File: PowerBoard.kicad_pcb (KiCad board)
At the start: 2 copper layers, 212 parts, among them Q1 PSMN020-100YS, Q2 PSMN020-100YS, Q3 PSMN020-100YS, Q4 PSMN020-100YS, Q5 PSMN020-100YS, U1 LT8342RV-TRMPBF, U10 LM5050-1, U11 PINA745AIRELR, U12 TPS16851VMAR, U13 LM5050-1, U14 TPS16851VMAR, U15 LM5050-1, U16 TPS16851VMAR, U17 LM5050-1, U18 LMR43620MSC5RPERQ1, U2 AD5259BRMZ100, U3 ADAFRUIT_QT_PY, U4 TPS16851VMAR, U5 LM5050-1, U6 LT8342RV-TRMPBF, U7 PINA745AIRELR, U8 AD5259BRMZ100, U9 TPS16851VMAR

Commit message: Starting bus load switch layout
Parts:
- removed D13, D17, D18, D5: TPSMB28CA-VR, Diode_SMD:D_SMB
- removed D15, D19, D20, D3, D7: BAT46GWJ, Diode_SMD:D_SOD-123
- removed L1: 33uH, _Power_Board:IND_SER2918H-333KL
- removed L3: 3.3uH, Inductor_SMD:L_Bourns_SRN6045TA
- removed Q3, Q4, Q5: PSMN020-100YS, Package_TO_SOT_SMD:LFPAK56
- removed R25: 274k, Resistor_SMD:R_0603_1608Metric
- removed R26, R39: 1Meg, Resistor_SMD:R_0603_1608Metric
- removed R38, R64: 100, Resistor_SMD:R_0603_1608Metric
- removed R40, R66: 36k, Resistor_SMD:R_0603_1608Metric
- removed R42, R68: 67.3k, Resistor_SMD:R_0603_1608Metric
- removed R44: 240k, Resistor_SMD:R_0603_1608Metric
- removed R45: 33k, Resistor_SMD:R_0603_1608Metric
- removed R49, R62: 1k, Resistor_SMD:R_0603_1608Metric
- removed R50, R63: 10, Resistor_SMD:R_1206_3216Metric
- removed R69: 150, Resistor_SMD:R_0603_1608Metric
- removed U1, U6: LT8342RV-TRMPBF, _Power_Board:05-08-7040_ADI
- removed U12, U4: TPS16851VMAR, _Power_Board:05-08-7040_ADI
- removed U17, U5: LM5050-1, Package_TO_SOT_SMD:TSOT-23-6
- removed U18: LMR43620MSC5RPERQ1, _Power_Board:RPE0009A-MFG
- removed U2: AD5259BRMZ100, _Power_Board:RM_10_ADI
- removed U3: ADAFRUIT_QT_PY, _Power_Board:MODULE_ADAFRUIT_QT_PY
- removed U7: PINA745AIRELR, _Power_Board:REL0014A_PINA745AIRELR_TEX
- added C86: 1uF, Capacitor_SMD:C_0603_1608Metric, F.Cu at (43.5, 77.2)
- added C87: 0.1uF, Capacitor_SMD:C_0603_1608Metric, F.Cu at (43.5, 79.7)
- added C88: 1uF, Capacitor_SMD:C_0603_1608Metric, F.Cu at (82.0, 76.0)
- added C89: 0.1uF, Capacitor_SMD:C_0603_1608Metric, F.Cu at (82.0, 78.5)
- added FB5: FerriteBead, Inductor_SMD:L_1812_4532Metric, F.Cu at (81.1, 52.4)
- added J1: Conn_01x02_Socket, Connector_JST:JST_PH_B2B-PH-K_1x02_P2.00mm_Vertical, F.Cu at (67.0, 87.3)
- added NT1: NetTie_2, NetTie:NetTie-2_SMD_Pad0.5mm, F.Cu at (173.8, 85.7)
- added NT2: NetTie_2, NetTie:NetTie-2_SMD_Pad0.5mm, F.Cu at (173.8, 87.2)
- added NT3: NetTie_2, NetTie:NetTie-2_SMD_Pad0.5mm, F.Cu at (88.7, -14.2)
- added NT4: NetTie_2, NetTie:NetTie-2_SMD_Pad0.5mm, F.Cu at (173.8, 98.5)
- added NT5: NetTie_2, NetTie:NetTie-2_SMD_Pad0.5mm, F.Cu at (173.8, 100.0)
- added NT6: NetTie_2, NetTie:NetTie-2_SMD_Pad0.5mm, F.Cu at (62.9, 47.2)
- added Q19: PSMN020-100YS, Package_TO_SOT_SMD:LFPAK56, F.Cu at (190.7, 104.0)
- added Q9: PSMN020-100YS, Package_TO_SOT_SMD:LFPAK56, F.Cu at (190.7, 91.2)
- added TP2: TP_PGOOD, TestPoint:TestPoint_Plated_Hole_D5.0mm, F.Cu at (210.1, 22.5)
- added TP3: TP_FLTn, TestPoint:TestPoint_Plated_Hole_D5.0mm, F.Cu at (220.7, 22.8)
- C19: value 100nF -> 100 nF; footprint Capacitor_SMD:C_1206_3216Metric -> Capacitor_SMD:C_0402_1005Metric
- C2: value 3.3nF -> 100nF
- C20: value 100pF -> 100 nF; footprint Capacitor_SMD:C_0603_1608Metric -> Capacitor_SMD:C_0402_1005Metric
- C21: value 10pF -> 100 nF; footprint Capacitor_SMD:C_0603_1608Metric -> Capacitor_SMD:C_0402_1005Metric
- C22: value 0.22uF -> 100 nF; footprint Capacitor_SMD:C_0603_1608Metric -> Capacitor_SMD:C_0402_1005Metric
- C23: value 4.7nF -> 100 nF; footprint Resistor_SMD:R_0603_1608Metric -> Capacitor_SMD:C_0402_1005Metric
- C24: value 22pF -> 100 nF; footprint Capacitor_SMD:C_0603_1608Metric -> Capacitor_SMD:C_0402_1005Metric
- C25: value 100pF -> 15p; footprint Capacitor_SMD:C_0603_1608Metric -> Resistor_SMD:R_0201_0603Metric
- C26: value 22nF -> 15p; footprint Capacitor_SMD:C_0805_2012Metric -> Resistor_SMD:R_0201_0603Metric
- C27: value 100nF -> 100 nF; footprint Capacitor_SMD:C_0805_2012Metric -> Capacitor_SMD:C_0402_1005Metric
- C28: value 220pF -> 100 nF; footprint Capacitor_SMD:C_0603_1608Metric -> Capacitor_SMD:C_0402_1005Metric
- C29: value 3.3nF -> 100 nF; footprint Capacitor_SMD:C_0603_1608Metric -> Capacitor_SMD:C_0402_1005Metric
- C3, C37: value 100nF -> 10uF; footprint Capacitor_SMD:C_0603_1608Metric -> Capacitor_SMD:C_0805_2012Metric
- C30, C32, C34: value 100nF -> 4.7u; footprint Capacitor_SMD:C_0603_1608Metric -> Capacitor_SMD:C_0402_1005Metric
- C31: value 2.2uF -> 100 nF; footprint Capacitor_SMD:C_0603_1608Metric -> Capacitor_SMD:C_0402_1005Metric
- C33: value 10uF -> 4.7u; footprint Capacitor_SMD:C_0805_2012Metric -> Capacitor_SMD:C_0402_1005Metric
- C35: value 33uF -> 220pF; footprint Capacitor_SMD:CP_Elec_6.3x5.8 -> Capacitor_SMD:C_0603_1608Metric
- C36, C41, C46: value 10uF -> 100nF; footprint Capacitor_SMD:C_0805_2012Metric -> Capacitor_SMD:C_0603_1608Metric
- C38: value 100nF -> 3.3nF
- C4: value 2.2uF -> 3.3nF
- C40, C6: value 10uF -> 2.2uF; footprint Capacitor_SMD:C_0805_2012Metric -> Capacitor_SMD:C_0603_1608Metric
- C42: value 100nF -> 33uF; footprint Capacitor_SMD:C_0603_1608Metric -> Capacitor_SMD:CP_Elec_6.3x5.8
- C43: value 220pF -> 10uF; footprint Capacitor_SMD:C_0603_1608Metric -> Capacitor_SMD:C_0805_2012Metric
- C47: value 100pF -> 10uF; footprint Capacitor_SMD:C_0603_1608Metric -> Capacitor_SMD:C_0805_2012Metric
- C48: value 10pF -> 10uF; footprint Capacitor_SMD:C_0603_1608Metric -> Capacitor_SMD:C_0805_2012Metric
- C49: value 0.22uF -> 100nF
- C50: value 4.7nF -> 220pF; footprint Resistor_SMD:R_0603_1608Metric -> Capacitor_SMD:C_0603_1608Metric
- C51: value 22pF -> 100nF
- C52: value 100pF -> 100nF
- C53: value 22nF -> 10uF
- C54: footprint Capacitor_SMD:C_0805_2012Metric -> Capacitor_SMD:C_0603_1608Metric
- C55: footprint Capacitor_SMD:C_0603_1608Metric -> Capacitor_SMD:C_0805_2012Metric
- C56: value 100pF -> 100nF; footprint Capacitor_SMD:C_0603_1608Metric -> Capacitor_SMD:C_0805_2012Metric
- C57: value 10pF -> 100nF; footprint Capacitor_SMD:C_0603_1608Metric -> Capacitor_SMD:C_0805_2012Metric
- C58: value 0.22uF -> 100pF; moved to B.Cu
- C59: value 4.7nF -> 10pF; footprint Resistor_SMD:R_0603_1608Metric -> Capacitor_SMD:C_0603_1608Metric; moved to B.Cu
- C60: value 22pF -> 0.22uF
- C61: value 100pF -> 4.7nF; footprint Capacitor_SMD:C_0603_1608Metric -> Resistor_SMD:R_0603_1608Metric; moved to B.Cu
- C62: value 22nF -> 22pF; footprint Capacitor_SMD:C_0805_2012Metric -> Capacitor_SMD:C_0603_1608Metric; moved to B.Cu
- C63: value 100nF -> 100pF; footprint Capacitor_SMD:C_0805_2012Metric -> Capacitor_SMD:C_0603_1608Metric; moved to B.Cu
- C64: value 100pF -> 22nF; footprint Capacitor_SMD:C_0603_1608Metric -> Capacitor_SMD:C_0805_2012Metric; moved to B.Cu
- C65: value 10pF -> 100nF; moved to B.Cu
- C66: value 0.22uF -> 10uf; footprint Capacitor_SMD:C_0603_1608Metric -> Capacitor_SMD:C_1210_3225Metric
- C67, C75: value 4.7nF -> 1uF; footprint Resistor_SMD:R_0603_1608Metric -> Capacitor_SMD:C_0603_1608Metric
- C68: value 22pF -> 10uf; footprint Capacitor_SMD:C_0603_1608Metric -> Capacitor_SMD:C_1210_3225Metric
- C69: value 100pF -> 10uf; footprint Capacitor_SMD:C_0603_1608Metric -> Capacitor_SMD:C_1210_3225Metric
- C70: value 22nF -> 1uF; footprint Capacitor_SMD:C_0805_2012Metric -> Capacitor_SMD:C_0603_1608Metric
- C71: value 100nF -> 1uF; footprint Capacitor_SMD:C_0805_2012Metric -> Capacitor_SMD:C_0603_1608Metric
- C72: value 100pF -> 1uF
- C73: value 10pF -> 10nF
- C74: value 0.22uF -> 0.1uF
- C76: value 22pF -> 4.7pF
- C77: value 100pF -> 47uF; footprint Capacitor_SMD:C_0603_1608Metric -> Capacitor_SMD:C_1210_3225Metric
- C78: value 22nF -> 100pF; footprint Capacitor_SMD:C_0805_2012Metric -> Capacitor_SMD:C_0603_1608Metric; moved to B.Cu
- C79: value 100nF -> 10pF; footprint Capacitor_SMD:C_0805_2012Metric -> Capacitor_SMD:C_0603_1608Metric; moved to B.Cu
- C80: value 4.7uF -> 0.22uF; footprint Capacitor_SMD:C_0805_2012Metric -> Capacitor_SMD:C_0603_1608Metric
- C81: value 100nF -> 4.7nF; footprint Capacitor_SMD:C_0603_1608Metric -> Resistor_SMD:R_0603_1608Metric; moved to B.Cu
- C82: value 1uF -> 22pF; footprint Capacitor_SMD:C_0805_2012Metric -> Capacitor_SMD:C_0603_1608Metric; moved to B.Cu
- C83: value 100nF -> 100pF; moved to B.Cu
- C84: value 22uF -> 22nF; footprint Capacitor_SMD:CP_Elec_6.3x5.9 -> Capacitor_SMD:C_0805_2012Metric; moved to B.Cu
- C85: value 22uF -> 100nF; footprint Capacitor_SMD:CP_Elec_6.3x5.9 -> Capacitor_SMD:C_0603_1608Metric; moved to B.Cu
- D10: value TPSMB28CA-VR -> SMF5.0A; footprint Diode_SMD:D_SMB -> Diode_SMD:D_SOD-123F
- D11, D12: value BAT46GWJ -> TPSMB28CA-VR; footprint Diode_SMD:D_SOD-123 -> Diode_SMD:D_SMB
- D14, D6: value TPSMB28CA-VR -> BAT46GWJ; footprint Diode_SMD:D_SMB -> Diode_SMD:D_SOD-123
- D8: value BAT46GWJ -> SMCJ26A; footprint Diode_SMD:D_SOD-123 -> Diode_SMD:D_SMC
- D9: value TPSMB28CA-VR -> SMF3.3; footprint Diode_SMD:D_SMB -> Diode_SMD:D_SOD-123F
- L2: value 33uH -> 3.3u; footprint _Power_Board:IND_SER2918H-333KL -> Inductor_SMD:L_0805_2012Metric
- Q1, Q2: value PSMN020-100YS -> Q_NMOS; footprint Package_TO_SOT_SMD:LFPAK56 -> Package_DFN_QFN:WDFN-8-1EP_2x2.2mm_P0.5mm_EP0.80x0.54
- R10: value 1Meg -> 33k; footprint Resistor_SMD:R_0603_1608Metric -> Resistor_SMD:R_0402_1005Metric
- R11: value 67.3k -> 1k; footprint Resistor_SMD:R_0603_1608Metric -> Resistor_SMD:R_0402_1005Metric
- R12: value 150 -> 1k; footprint Resistor_SMD:R_0603_1608Metric -> Resistor_SMD:R_0201_0603Metric
- R13: value 240k -> 1k; footprint Resistor_SMD:R_0603_1608Metric -> Resistor_SMD:R_0402_1005Metric
- R14, R15: value 33k -> 27; footprint Resistor_SMD:R_0603_1608Metric -> Resistor_SMD:R_0201_0603Metric
- R16: value 1.26k -> 33; footprint Resistor_SMD:R_0603_1608Metric -> Resistor_SMD:R_0402_1005Metric
- R17: value 464 -> 33.6k
- R18: value 1k -> 60.4k
- R19: value 10 -> 33.6k; footprint Resistor_SMD:R_1206_3216Metric -> Resistor_SMD:R_0603_1608Metric
- R20: value 100 -> R_US
- R21: value 33.6k -> 274k
- R22: value 60.4k -> 15k
- R23: value 33.6k -> 33k
- R24: value 15k -> 33k
- R27, R53: value 36k -> 1Meg; moved to B.Cu
- R28, R52: value 1Meg -> 36k; moved to B.Cu
- R29: value 67.3k -> 1Meg; moved to B.Cu
- R30: value 150 -> 67.3k; moved to B.Cu
- R31: value 240k -> 150
- R32: value 33k -> 240k; moved to B.Cu
- R33, R58, U10: moved to B.Cu
- R34: value 1.26k -> 33k; moved to B.Cu
- R35: value 464 -> 1.26k; moved to B.Cu
- R36: value 1k -> 464; moved to B.Cu
- R37: value 10 -> 1k; footprint Resistor_SMD:R_1206_3216Metric -> Resistor_SMD:R_0603_1608Metric; moved to B.Cu
- R4: value 15k -> R_US
- R41, R65: value 1Meg -> 10; footprint Resistor_SMD:R_0603_1608Metric -> Resistor_SMD:R_1206_3216Metric
- R43: value 150 -> 100; moved to B.Cu
- R46: value 33k -> 18.22K
- R47: value 1.26k -> 1M
- R48: value 464 -> 243k
- R51: value 100 -> 1Meg; moved to B.Cu
- R54: value 1Meg -> 67.3k; moved to B.Cu
- R55: value 67.3k -> 150
- R56: value 150 -> 240k; moved to B.Cu
- R57: value 240k -> 33k; moved to B.Cu
- R59: value 33k -> 1.26k; moved to B.Cu
- R6: value 33k -> 15k
- R60: value 1.26k -> 464; moved to B.Cu
- R61: value 464 -> 1k; moved to B.Cu
- R67: value 1Meg -> 100; moved to B.Cu
- R7: value 33k -> 100; footprint Resistor_SMD:R_0603_1608Metric -> Resistor_SMD:R_0201_0603Metric
- R70: value 240k -> 402k
- R71: value 33k -> 12k
- R72: value 33k -> R_US
- R73: value 1.26k -> 33k
- R74: value 464 -> 402k
- R75: value 1k -> 12k
- R76: value 10 -> R_US; footprint Resistor_SMD:R_1206_3216Metric -> Resistor_SMD:R_0603_1608Metric
- R77: value 100 -> 33k
- R8: value 1Meg -> 100; footprint Resistor_SMD:R_0603_1608Metric -> Resistor_SMD:R_0201_0603Metric
- R9: value 36k -> 33k; footprint Resistor_SMD:R_0603_1608Metric -> Resistor_SMD:R_0402_1005Metric
- U11: value PINA745AIRELR -> TLV75533PDBV; footprint _Power_Board:REL0014A_PINA745AIRELR_TEX -> Package_TO_SOT_SMD:SOT-23-5
- U13: value LM5050-1 -> TPS16851VMAR; footprint Package_TO_SOT_SMD:TSOT-23-6 -> _PowerBoard:VMA0023A-MFG
- U14: value TPS16851VMAR -> LM5050-1; footprint _Power_Board:05-08-7040_ADI -> Package_TO_SOT_SMD:TSOT-23-6; moved to B.Cu
- U15: value LM5050-1 -> TPS26400PWP; footprint Package_TO_SOT_SMD:TSOT-23-6 -> Package_DFN_QFN:VQFN-24-1EP_4x4mm_P0.5mm_EP2.45x2.45mm_ThermalVias
- U16: value TPS16851VMAR -> TPS26400PWP; footprint _Power_Board:05-08-7040_ADI -> Package_DFN_QFN:VQFN-24-1EP_4x4mm_P0.5mm_EP2.45x2.45mm_ThermalVias
- U8: value AD5259BRMZ100 -> BNO055; footprint _Power_Board:RM_10_ADI -> Package_LGA:LGA-28_5.2x3.8mm_P0.5mm
- U9: footprint _Power_Board:05-08-7040_ADI -> _PowerBoard:VMA0023A-MFG
- moved C18 221.3 mm to (-21.4, 50.6)
- moved R5 220.5 mm to (-25.6, 52.9)
- moved C17 219.7 mm to (-25.6, 50.4)
- moved R6 211.9 mm to (-25.6, 55.4)
- moved R21 206.4 mm to (-25.6, 62.4)
- moved R22 206.4 mm to (-25.6, 64.9)
- moved C53 180.6 mm to (-21.4, 60.1)
- moved C54 176.8 mm to (-19.6, 69.4)
- moved C55 172.0 mm to (21.3, 77.4)
- moved C52 170.7 mm to (-25.6, 59.9)
- moved U8 169.5 mm to (27.1, 78.8)
- moved R4 167.7 mm to (29.1, 56.2)
- moved C44 167.1 mm to (47.5, 51.2)
- moved C51 165.6 mm to (-25.6, 69.4)
- moved R24 163.9 mm to (25.5, 85.3)
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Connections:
- net /Main/BOOSTX.TEMP renamed /Main/batt1_lsw/TEMP
- C15 pad 1: /Main/boost_a_frontend/BOOST_OUT -> VBUS
- C16 pad 2: /Main/boost_a_frontend/BOOST_OUT -> VBUS
- C19 pad 1: +5V -> +3V3
- C2 pad 2: Net-(C2-Pad2) -> /Main/boost_a_frontend/PANEL_IN
- C20 pad 1: Net-(U4-OVP) -> +1V1
- C21 pad 1: Net-(U4-EN_UVLO) -> +3V3
- C22 pad 1: Net-(U4-VDD) -> +3V3
- C23 pad 1: Net-(U4-ITIMER) -> +1V1
- C24 pad 1: Net-(U4-ILIM) -> +3V3
- C25 pad 1: Net-(U4-IREF) -> /Main/mcu/XIN
- C26 pad 1: Net-(U4-dVdT) -> /Main/mcu/XR
- C27 pad 1: Net-(U5-VS) -> GND
- C27 pad 2: GND -> +3V3
- C28 pad 2: /Main/boost_b_frontend/PANEL_IN -> +1V1
- C29 pad 2: Net-(C29-Pad2) -> +3V3
- C3 pad 2: Net-(U1-SS) -> /Main/boost_a_frontend/PANEL_IN
- C30 pad 1: GND -> +3V3
- C30 pad 2: Net-(U6-SS) -> GND
- C31 pad 2: /Main/boost_b_frontend/INTVCC -> +3V3
- C32 pad 1: GND -> Net-(U3-VREG_AVDD)
- C32 pad 2: /Main/boost_b_frontend/PANEL_IN -> GND
- C33 pad 2: /Main/boost_b_frontend/PANEL_IN -> +1V1
- C34 pad 2: Net-(U6-VIN) -> +3V3
- C35 pad 1: Net-(U6-VIN) -> GND
- C35 pad 2: GND -> /Main/boost_b_frontend/PANEL_IN
- C36 pad 2: Net-(U6-VIN) -> /Main/boost_b_frontend/PANEL_IN
- C37 pad 1: Net-(C37-Pad1) -> GND
- C37 pad 2: Net-(U6-BST) -> /Main/boost_b_frontend/PANEL_IN
- C38 pad 1: /Main/boost_b_frontend/Vout -> GND
- C38 pad 2: GND -> Net-(C38-Pad2)
- C39 pad 1: /Main/boost_b_frontend/Vout -> GND
- C39 pad 2: GND -> Net-(U4-SS)
- C4 pad 2: /Main/boost_a_frontend/INTVCC -> Net-(C4-Pad2)
- C40 pad 2: /Main/boost_b_frontend/Vout -> /Main/boost_b_frontend/INTVCC
- C41 pad 2: /Main/boost_b_frontend/Vout -> Net-(U4-VIN)
- C42 pad 1: /Main/boost_b_frontend/BOOST_OUT -> Net-(U4-VIN)
- C43 pad 2: /Main/boost_b_frontend/BOOST_OUT -> Net-(U4-VIN)
- C44 pad 1: GND -> Net-(C44-Pad1)
- C44 pad 2: +5V -> Net-(U4-BST)
- C45 pad 1: +5V -> /Main/boost_b_frontend/Vout
- C46 pad 1: +5V -> /Main/boost_b_frontend/Vout
- C47 pad 1: Net-(U9-OVP) -> GND
- C47 pad 2: GND -> /Main/boost_b_frontend/Vout
- C48 pad 1: Net-(U9-EN_UVLO) -> GND
- C48 pad 2: GND -> /Main/boost_b_frontend/Vout
- C49 pad 1: Net-(U9-VDD) -> VBUS
- C5 pad 2: /Main/boost_a_frontend/PANEL_IN -> Net-(U1-SS)
- C50 pad 1: Net-(U9-ITIMER) -> GND
- C50 pad 2: GND -> VBUS
- C51 pad 1: Net-(U9-ILIM) -> GND
- C51 pad 2: GND -> +5V
- C52 pad 1: Net-(U9-IREF) -> +5V
- C53 pad 1: Net-(U9-dVdT) -> +5V
- C54 pad 1: Net-(U10-VS) -> GND
- C54 pad 2: GND -> +5V
- C55 pad 1: GND -> LVBUS_3V3
- C55 pad 2: +5V -> GND
- C56 pad 1: Net-(U12-OVP) -> LVBUS_3V3
- C57 pad 1: Net-(U12-EN_UVLO) -> Net-(U8-CAP)
- C58 pad 1: Net-(U12-VDD) -> Net-(U9-OVP)
- C59 pad 1: Net-(U12-ITIMER) -> /Main/batt1_lsw/EN_UVLO
- C6 pad 2: /Main/boost_a_frontend/PANEL_IN -> /Main/boost_a_frontend/INTVCC
- C60 pad 1: Net-(U12-ILIM) -> Net-(U9-VDD)
- C61 pad 1: Net-(U12-IREF) -> Net-(U9-ITIMER)
- C62 pad 1: Net-(U12-dVdT) -> Net-(U9-ILIM)
- C63 pad 1: Net-(U13-VS) -> Net-(U9-IREF)
- C64 pad 1: Net-(U14-OVP) -> Net-(U9-dVdT)
- C65 pad 1: Net-(U14-EN_UVLO) -> Net-(U10-VS)
- C66 pad 1: Net-(U14-VDD) -> /Main/LV_BUS/HV_BUS
- C67 pad 1: Net-(U14-ITIMER) -> /Main/LV_BUS/LV_BUS_5V
- C68 pad 1: Net-(U14-ILIM) -> Net-(U12-EN)
- C69 pad 1: Net-(U14-IREF) -> Net-(U12-EN)
- C70 pad 1: Net-(U14-dVdT) -> Net-(U12-EN)
- C71 pad 1: Net-(U15-VS) -> /Main/LV_BUS/LVBUS_3V3
- C72 pad 1: Net-(U16-OVP) -> Net-(U12-EN)
- C73 pad 1: Net-(U16-EN_UVLO) -> Net-(U12-TR/SS)
- C74 pad 1: Net-(U16-VDD) -> Net-(U12-BST)
- C74 pad 2: GND -> Net-(C74-Pad2)
- C75 pad 1: Net-(U16-ITIMER) -> Net-(U12-INTVCC)
- C76 pad 1: Net-(U16-ILIM) -> /Main/LV_BUS/LVBUS_5V
- C76 pad 2: GND -> Net-(U12-FB)
- C77 pad 1: Net-(U16-IREF) -> /Main/LV_BUS/LVBUS_5V
- C78 pad 1: Net-(U16-dVdT) -> Net-(U13-OVP)
- C79 pad 1: Net-(U17-VS) -> /Main/batt2_lsw/EN_UVLO
- C80 pad 1: VBUS -> Net-(U13-VDD)
- C81 pad 1: VBUS -> Net-(U13-ITIMER)
- C82 pad 1: Net-(U18-VCC) -> Net-(U13-ILIM)
- C83 pad 1: Net-(U18-BOOT) -> Net-(U13-IREF)
- C83 pad 2: Net-(U18-SW) -> GND
- C84 pad 1: +5V -> Net-(U13-dVdT)
- C85 pad 1: +5V -> Net-(U14-VS)
- D1 pad 2: /Main/boost_b_frontend/BOOST_OUT -> VBUS
- D10 pad 1: GND -> /Main/LV_BUS/LVBUS_5V
- D10 pad 2: Net-(D10-A2) -> GND
- D11 pad 1: Net-(D10-A2) -> GND
- D11 pad 2: GND -> VBUS
- D12 pad 1: VBUS -> GND
- D12 pad 2: GND -> /Main/batt2_lsw/BUS
- D14 pad 1: GND -> /Main/batt2_lsw/BUS
- D14 pad 2: Net-(D14-A2) -> GND
- D16 pad 1: VBUS -> /Main/batt2_lsw/OUT
- D2 pad 2: Net-(D2-A2) -> /Main/batt1_lsw/BUS
- D4 pad 1: VBUS -> /Main/batt1_lsw/BUS
- D6 pad 1: GND -> /Main/batt1_lsw/OUT
- D6 pad 2: Net-(D6-A2) -> GND
- D8 pad 1: VBUS -> /Main/LV_BUS/HV_BUS
- D9 pad 1: GND -> /Main/LV_BUS/LVBUS_3V3
- D9 pad 2: /Main/batt1_load_sw/IN -> GND
- FB2 pad 2: /Main/boost_a_frontend/BOOST_OUT -> VBUS
- FB3 pad 2: Net-(U6-VIN) -> Net-(U4-VIN)
- FB4 pad 2: /Main/boost_b_frontend/BOOST_OUT -> VBUS
- L2 pad 1: Net-(U6-VIN) -> Net-(U3-VREG_LX)
- L2 pad 2: Net-(C37-Pad1) -> +1V1
- R10 pad 1: /Main/boost_b_frontend/BOOST_OUT -> /Main/mcu/SCL
- R10 pad 2: Net-(U4-EN_UVLO) -> GND
- R11 pad 1: Net-(U4-EN_UVLO) -> /Main/mcu/RUN
- R11 pad 2: GND -> Net-(U3-RUN)
- R12 pad 1: /Main/boost_b_frontend/BOOST_OUT -> /Main/mcu/XOUT
- R12 pad 2: Net-(U4-VDD) -> /Main/mcu/XR
- R13 pad 1: Net-(U4-SFT_SEL) -> /Main/mcu/QSPI_SS
- R13 pad 2: GND -> /Main/mcu/BOOT
- R14 pad 1: /Main/BOOSTY.PGOOD -> /Main/mcu/D+
- R14 pad 2: +5V -> /Main/mcu/USB_D+
- R15 pad 1: /Main/BOOSTY.FLTn -> /Main/mcu/D-
- R15 pad 2: +5V -> /Main/mcu/USB_D-
- R16 pad 1: /Main/BOOSTY.IMON -> +3V3
- R16 pad 2: GND -> Net-(U3-VREG_AVDD)
- R17 pad 1: Net-(U4-ILIM) -> GND
- R17 pad 2: GND -> Net-(U4-RT)
- R18 pad 1: Net-(U4-IREF) -> Net-(C38-Pad2)
- R18 pad 2: GND -> Net-(U4-VC)
- R19 pad 1: Net-(Q1-PadG) -> /Main/boost_b_frontend/INTVCC
- R2 pad 1: Net-(C2-Pad2) -> Net-(C4-Pad2)
- R20 pad 1: Net-(U5-VS) -> Net-(U4-VIN)
- R21 pad 1: GND -> Net-(U6-A)
- R21 pad 2: Net-(U6-RT) -> /Main/SY_B.FB
- R22 pad 1: Net-(C29-Pad2) -> Net-(U6-B)
- R22 pad 2: Net-(U6-VC) -> GND
- R23 pad 1: /Main/boost_b_frontend/INTVCC -> +3.3V
- R23 pad 2: Net-(U6-VSET1) -> /Main/SDA
- R24 pad 1: Net-(U8-A) -> /Main/SCL
- R24 pad 2: /Main/SY_B.FB -> +3.3V
- R27 pad 1: Net-(U9-OVP) -> VBUS
- R27 pad 2: GND -> Net-(U9-OVP)
- R28 pad 1: /Main/boost_a_frontend/BOOST_OUT -> Net-(U9-OVP)
- R28 pad 2: Net-(U9-EN_UVLO) -> GND
- R29 pad 1: Net-(U9-EN_UVLO) -> VBUS
- R29 pad 2: GND -> /Main/batt1_lsw/EN_UVLO
- R30 pad 1: /Main/boost_a_frontend/BOOST_OUT -> /Main/batt1_lsw/EN_UVLO
- R30 pad 2: Net-(U9-VDD) -> GND
- R31 pad 1: Net-(U9-SFT_SEL) -> VBUS
- R31 pad 2: GND -> Net-(U9-VDD)
- R32 pad 1: /Main/BOOSTX.PGOOD -> Net-(U9-SFT_SEL)
- R32 pad 2: +5V -> GND
- R33 pad 1: /Main/BOOSTX.FLTn -> /Main/batt1_lsw/PGOOD
- R33 pad 2: +5V -> +3V3
- R34 pad 1: /Main/BOOSTX.IMON -> /Main/batt1_lsw/FLTn
- R34 pad 2: GND -> +3V3
- R35 pad 1: Net-(U9-ILIM) -> /Main/batt1_lsw/IMON
- R36 pad 1: Net-(U9-IREF) -> Net-(U9-ILIM)
- R37 pad 1: Net-(Q2-PadG) -> Net-(U9-IREF)
- R37 pad 2: Net-(U10-GATE) -> GND
- R4 pad 1: Net-(U2-A) (its old number) -> Net-(U1-VIN)
- R4 pad 2: /Main/SX_B.FB -> Net-(U1-SNS)
- R41 pad 1: /Main/batt1_load_sw/IN -> Net-(Q9-PadG)
- R41 pad 2: Net-(U12-EN_UVLO) -> Net-(U10-GATE)
- R43 pad 1: /Main/batt1_load_sw/IN -> Net-(U10-VS)
- R43 pad 2: Net-(U12-VDD) -> Net-(NT3-Pad1)
- R46 pad 1: /Main/BATT1.FLTn -> Net-(U12-RT)
- R46 pad 2: +5V -> GND
- R47 pad 1: /Main/BATT1.IMON -> /Main/LV_BUS/LVBUS_5V
- R47 pad 2: GND -> Net-(U12-FB)
- R48 pad 1: Net-(U12-ILIM) -> GND
- R48 pad 2: GND -> Net-(U12-FB)
- R5 pad 2: GND -> /Main/SX_B.FB
- R51 pad 1: Net-(U13-VS) -> VBUS
- R51 pad 2: Net-(NT9-Pad1) -> Net-(U13-OVP)
- R52 pad 1: /Main/batt2_load_sw/IN -> Net-(U13-OVP)
- R52 pad 2: Net-(U14-OVP) -> GND
- R53 pad 1: Net-(U14-OVP) -> VBUS
- R53 pad 2: GND -> /Main/batt2_lsw/EN_UVLO
- R54 pad 1: /Main/batt2_load_sw/IN -> /Main/batt2_lsw/EN_UVLO
- R54 pad 2: Net-(U14-EN_UVLO) -> GND
- R55 pad 1: Net-(U14-EN_UVLO) -> VBUS
- R55 pad 2: GND -> Net-(U13-VDD)
- R56 pad 1: /Main/batt2_load_sw/IN -> Net-(U13-SFT_SEL)
- R56 pad 2: Net-(U14-VDD) -> GND
- R57 pad 1: Net-(U14-SFT_SEL) -> /Main/batt2_lsw/PGOOD
- R57 pad 2: GND -> +3V3
- R58 pad 1: /Main/BATT2.PGOOD -> /Main/batt2_lsw/FLTn
- R58 pad 2: +5V -> +3V3
- R59 pad 1: /Main/BATT2.FLTn -> /Main/batt2_lsw/IMON
- R59 pad 2: +5V -> GND
- R6 pad 1: +5V -> Net-(U2-B)
- R6 pad 2: /Main/SDA -> GND
- R60 pad 1: /Main/BATT2.IMON -> Net-(U13-ILIM)
- R61 pad 1: Net-(U14-ILIM) -> Net-(U13-IREF)
- R65 pad 1: /Main/batt3_load_sw/IN -> Net-(Q19-PadG)
- R65 pad 2: Net-(U16-OVP) -> Net-(U14-GATE)
- R67 pad 1: /Main/batt3_load_sw/IN -> Net-(U14-VS)
- R67 pad 2: Net-(U16-EN_UVLO) -> Net-(NT6-Pad1)
- R7 pad 1: /Main/SCL -> /Main/mcu/SWCLK
- R7 pad 2: +5V -> /Main/mcu/SWCLK_INT
- R70 pad 1: Net-(U16-SFT_SEL) -> /Main/navlight_load_sw2/RTN
- R70 pad 2: GND -> Net-(U15-MODE)
- R71 pad 1: /Main/BATT3.PGOOD -> GND
- R71 pad 2: +5V -> Net-(U15-ILIM)
- R72 pad 1: /Main/BATT3.FLTn -> /Main/navlight_load_sw2/IMON
- R72 pad 2: +5V -> GND
- R73 pad 1: /Main/BATT3.IMON -> +3V3
- R73 pad 2: GND -> /Main/navlight_load_sw2/nFLT
- R74 pad 1: Net-(U16-ILIM) -> /Main/navlight_load_sw1/RTN
- R74 pad 2: GND -> Net-(U16-MODE)
- R75 pad 1: Net-(U16-IREF) -> GND
- R75 pad 2: GND -> Net-(U16-ILIM)
- R76 pad 1: Net-(Q5-PadG) -> /Main/navlight_load_sw1/IMON
- R76 pad 2: Net-(U17-GATE) -> GND
- R77 pad 1: Net-(U17-VS) -> +3V3
- R77 pad 2: Net-(NT15-Pad1) -> /Main/navlight_load_sw1/nFLT
- R8 pad 1: /Main/boost_b_frontend/BOOST_OUT -> /Main/mcu/SWDIO_INT
- R8 pad 2: Net-(U4-OVP) -> /Main/mcu/SWDIO
- R9 pad 1: Net-(U4-OVP) -> GND
- R9 pad 2: GND -> /Main/mcu/SDA
- U10 pad 3: GND -> /Main/batt1_lsw/EN_DIODE
- U11 pad 1: Net-(U11-IN+) -> /Main/LV_BUS/LV_BUS_5V
- U11 pad 2: Net-(U11-IN+) -> GND
- U11 pad 3: GND -> /Main/LV_BUS/LV_BUS_5V
- U11 pad 4: GND -> unconnected-(U11-NC-Pad4)
- U11 pad 5: /Main/SDA -> /Main/LV_BUS/LVBUS_3V3
- U13 pad 1: Net-(U13-VS) -> Net-(U13-ILIM)
- U13 pad 2: GND -> /Main/batt2_lsw/IMON
- U13 pad 3: GND -> Net-(U13-IREF)
- U13 pad 4: Net-(U13-IN) -> Net-(U13-dVdT)
- U13 pad 5: Net-(U13-GATE) -> GND
- U13 pad 6: Net-(U13-OUT) -> Net-(U13-SFT_SEL)
- U14 pad 1: Net-(U14-ILIM) -> Net-(U14-VS)
- U14 pad 2: /Main/BATT2.IMON -> GND
- U14 pad 3: Net-(U14-IREF) -> /Main/batt2_lsw/EN_DIODE
- U14 pad 4: Net-(U14-dVdT) -> Net-(U14-IN)
- U14 pad 5: GND -> Net-(U14-GATE)
- U14 pad 6: Net-(U14-SFT_SEL) -> Net-(U14-OUT)
- U15 pad 1: Net-(U15-VS) -> VBUS
- U15 pad 2: GND -> VBUS
- U15 pad 3: GND -> /Main/navlight_load_sw2/RTN
- U15 pad 4: Net-(U15-IN) -> unconnected-(U15-NC-Pad4)
- U15 pad 5: Net-(U15-GATE) -> /Main/navlight_load_sw2/RTN
- U15 pad 6: Net-(U15-OUT) -> Net-(U15-MODE)
- U16 pad 1: Net-(U16-ILIM) -> VBUS
- U16 pad 10: /Main/batt3_load_sw/IN -> /Main/navlight_load_sw1/IMON
- U16 pad 11: unconnected-(U16-NC-Pad11) -> Net-(U16-ILIM)
- U16 pad 12: unconnected-(U16-MODE-Pad12) -> Net-(U16-dVdT)
- U16 pad 13: /Main/BATT3.FLTn -> unconnected-(U16-NC-Pad13)
- U16 pad 14: Net-(U16-ITIMER) -> /Main/navlight_load_sw1/nFLT
- U16 pad 15: /Main/BATT3.TEMP -> /Main/navlight_load_sw1/OUTPUT
- U16 pad 16: Net-(U16-EN_UVLO) -> /Main/navlight_load_sw1/OUTPUT
- U16 pad 17: unconnected-(U16-NC-Pad17) -> /Main/navlight_load_sw1/RTN
- U16 pad 18: Net-(U16-OVP) -> (no net)
- U16 pad 19: /Main/BATT3.PGOOD -> (no net)
- U16 pad 2: /Main/BATT3.IMON -> VBUS
- U16 pad 20: /Main/BATT3.EN -> (no net)
- U16 pad 21: unconnected-(U16-NC-Pad21) -> (no net)
- U16 pad 22: /Main/batt3_load_sw/IN -> (no net)
- U16 pad 23: /Main/batt3_load_sw/IN -> (no net)
- U16 pad 24: /Main/batt3_load_sw/IN -> (no net)
- U16 pad 3: Net-(U16-IREF) -> /Main/navlight_load_sw1/RTN
- U16 pad 4: Net-(U16-dVdT) -> unconnected-(U16-NC-Pad4)
- U16 pad 5: GND -> /Main/navlight_load_sw1/RTN
- U16 pad 6: Net-(U16-SFT_SEL) -> Net-(U16-MODE)
- U16 pad 7: Net-(D18-A2) -> /Main/navlight_load_sw1/GPIO_IN
- U16 pad 8: Net-(D18-A2) -> /Main/navlight_load_sw1/RTN
- U16 pad 9: Net-(U16-VDD) -> GND
- U8 pad 1: Net-(U8-A) -> unconnected-(U8-PIN1-Pad1)
- U8 pad 10: Net-(U8-A) -> unconnected-(U8-BL_IND-Pad10)
- U8 pad 2: unconnected-(U8-AD0-Pad2) -> GND
- U8 pad 3: unconnected-(U8-AD1-Pad3) -> LVBUS_3V3
- U8 pad 4: /Main/SDA -> LVBUS_3V3
- U8 pad 5: /Main/SCL -> GND
- U8 pad 6: +5V -> GND
- U8 pad 7: GND -> unconnected-(U8-PIN7-Pad7)
- U8 pad 8: +5V -> unconnected-(U8-PIN8-Pad8)
- U8 pad 9: Net-(U8-B) -> Net-(U8-CAP)
- U9 pad 10: /Main/boost_a_frontend/BOOST_OUT -> VBUS
- U9 pad 13: /Main/BOOSTX.FLTn -> /Main/batt1_lsw/FLTn
- U9 pad 16: Net-(U9-EN_UVLO) -> /Main/batt1_lsw/EN_UVLO
- U9 pad 19: /Main/BOOSTX.PGOOD -> /Main/batt1_lsw/PGOOD
- U9 pad 2: /Main/BOOSTX.IMON -> /Main/batt1_lsw/IMON
- U9 pad 20: /Main/BOOSTX.EN -> unconnected-(U9-SWEN-Pad20)
- U9 pad 22: /Main/boost_a_frontend/BOOST_OUT -> VBUS
- U9 pad 23: /Main/boost_a_frontend/BOOST_OUT -> VBUS
- U9 pad 24: /Main/boost_a_frontend/BOOST_OUT -> VBUS
- U9 pad 7: Net-(D6-A2) -> /Main/batt1_lsw/BUS
- U9 pad 8: Net-(D6-A2) -> /Main/batt1_lsw/BUS

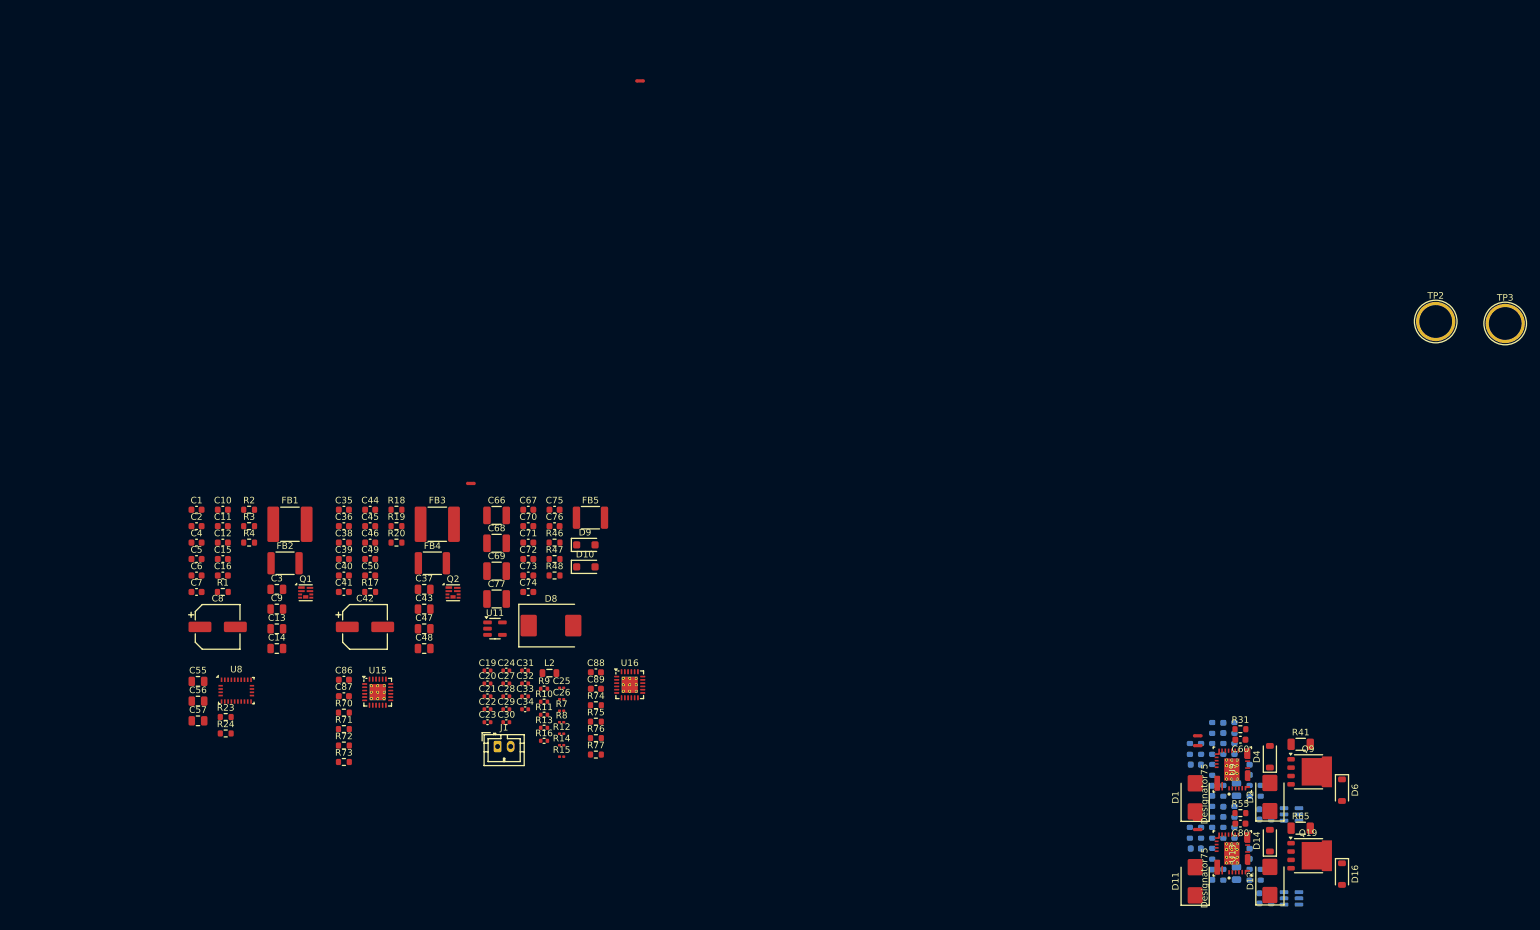
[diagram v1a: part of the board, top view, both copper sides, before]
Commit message: Laying out NavLight LSW & fixing up bus LSW
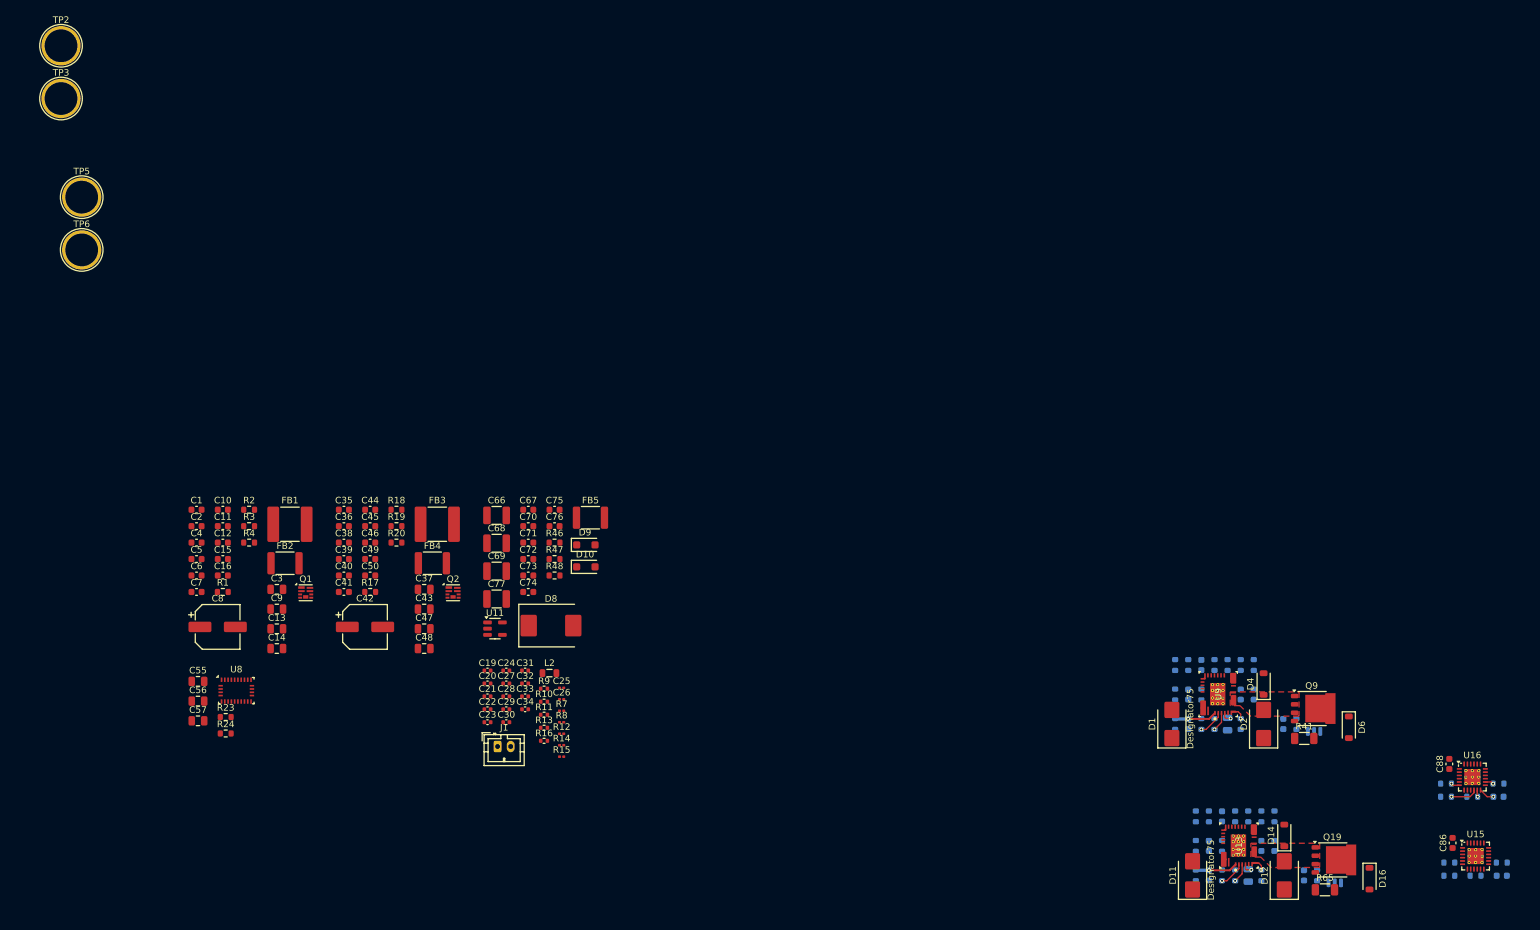
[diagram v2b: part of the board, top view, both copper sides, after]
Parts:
- removed NT1, NT2, NT3, NT4, NT5, NT6: NetTie_2, NetTie:NetTie-2_SMD_Pad0.5mm
- added TP5: TP_PGOOD, TestPoint:TestPoint_Plated_Hole_D5.0mm, F.Cu at (3.52, 3.52)
- added TP6: TP_FLTn, TestPoint:TestPoint_Plated_Hole_D5.0mm, F.Cu at (3.52, 11.6)
- C60, C80, C87, C89, R31, R55, R70, R71, R72, R73, R74, R75, R76, R77: moved to B.Cu
- Q19, Q9: footprint Package_TO_SOT_SMD:LFPAK56 -> _PowerBoard:LFPAK56_1
- moved TP3 223.0 mm to (0.37, -11.5)
- moved TP2 213.9 mm to (0.37, -19.6)
- moved C87 178.8 mm to (220.2, 107.1)
- moved R73 177.3 mm to (220.2, 105.1), turned to 180 degrees
- moved R71 174.1 mm to (216.2, 107.1)
- moved C86 171.0 mm to (212.7, 102.1), turned to 90 degrees
- moved R70 170.2 mm to (212.2, 105.1)
- moved R72 169.8 mm to (212.2, 107.1), turned to 180 degrees
- moved U15 169.4 mm to (216.2, 104.1)
- moved C89 138.7 mm to (219.7, 95.0)
- moved R77 137.8 mm to (219.7, 93.0), turned to 180 degrees
- moved R75 134.2 mm to (215.7, 95.0)
- moved C88 130.9 mm to (212.2, 90.0), turned to 90 degrees
- moved R74 130.3 mm to (211.7, 93.0)
- moved R76 130.0 mm to (211.7, 95.0), turned to 180 degrees
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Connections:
- Q19 pad 1: (no net) -> /Main/batt2_lsw/OUT
- Q19 pad 2: (no net) -> Net-(Q19-G)
- Q19 pad 3: (no net) -> /Main/batt2_lsw/BUS
- Q9 pad 1: (no net) -> /Main/batt1_lsw/OUT
- Q9 pad 2: (no net) -> Net-(Q9-G)
- Q9 pad 3: (no net) -> /Main/batt1_lsw/BUS
- R41 pad 1: Net-(Q9-PadG) -> Net-(Q9-G)
- R43 pad 2: Net-(NT3-Pad1) -> /Main/batt1_lsw/OUT
- R65 pad 1: Net-(Q19-PadG) -> Net-(Q19-G)
- R67 pad 2: Net-(NT6-Pad1) -> /Main/batt2_lsw/OUT
- U10 pad 4: Net-(U10-IN) -> /Main/batt1_lsw/BUS
- U10 pad 6: Net-(U10-OUT) -> /Main/batt1_lsw/OUT
- U14 pad 4: Net-(U14-IN) -> /Main/batt2_lsw/BUS
- U14 pad 6: Net-(U14-OUT) -> /Main/batt2_lsw/OUT
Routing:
- net Net-(U9-ILIM): track 0.00 -> 6.47 mm, vias 0 -> 1
- net Net-(U13-ILIM): track 0.00 -> 6.47 mm, vias 0 -> 1
- net /Main/navlight_load_sw1/IMON: track 0.00 -> 4.09 mm, vias 0 -> 1
- net /Main/batt1_lsw/IMON: track 0.00 -> 3.99 mm, vias 0 -> 1
- net /Main/batt2_lsw/IMON: track 0.00 -> 3.99 mm, vias 0 -> 1
- net Net-(U9-IREF): track 0.00 -> 2.95 mm, vias 0 -> 1
- net Net-(U13-IREF): track 0.00 -> 2.95 mm, vias 0 -> 1
- net Net-(U9-SFT_SEL): track 0.00 -> 2.71 mm, vias 0 -> 1
- net Net-(U13-SFT_SEL): track 0.00 -> 2.71 mm, vias 0 -> 1
- net Net-(U16-dVdT): track 0.00 -> 2.38 mm, vias 0 -> 1
- net Net-(U13-dVdT): track 0.00 -> 1.62 mm, vias 0 -> 1
- net Net-(U9-dVdT): track 0.00 -> 1.62 mm, vias 0 -> 1
- net Net-(U16-MODE): track 0.00 -> 1.30 mm, vias 0 -> 1
- net /Main/navlight_load_sw1/nFLT: track 0.00 -> 1.28 mm, vias 0 -> 1
- net Net-(U16-ILIM): track 0.00 -> 1.04 mm, vias 0 -> 1
- added copper zone on F.Cu, net /Main/batt1_lsw/BUS
- added copper zone on F.Cu, net /Main/batt2_lsw/BUS

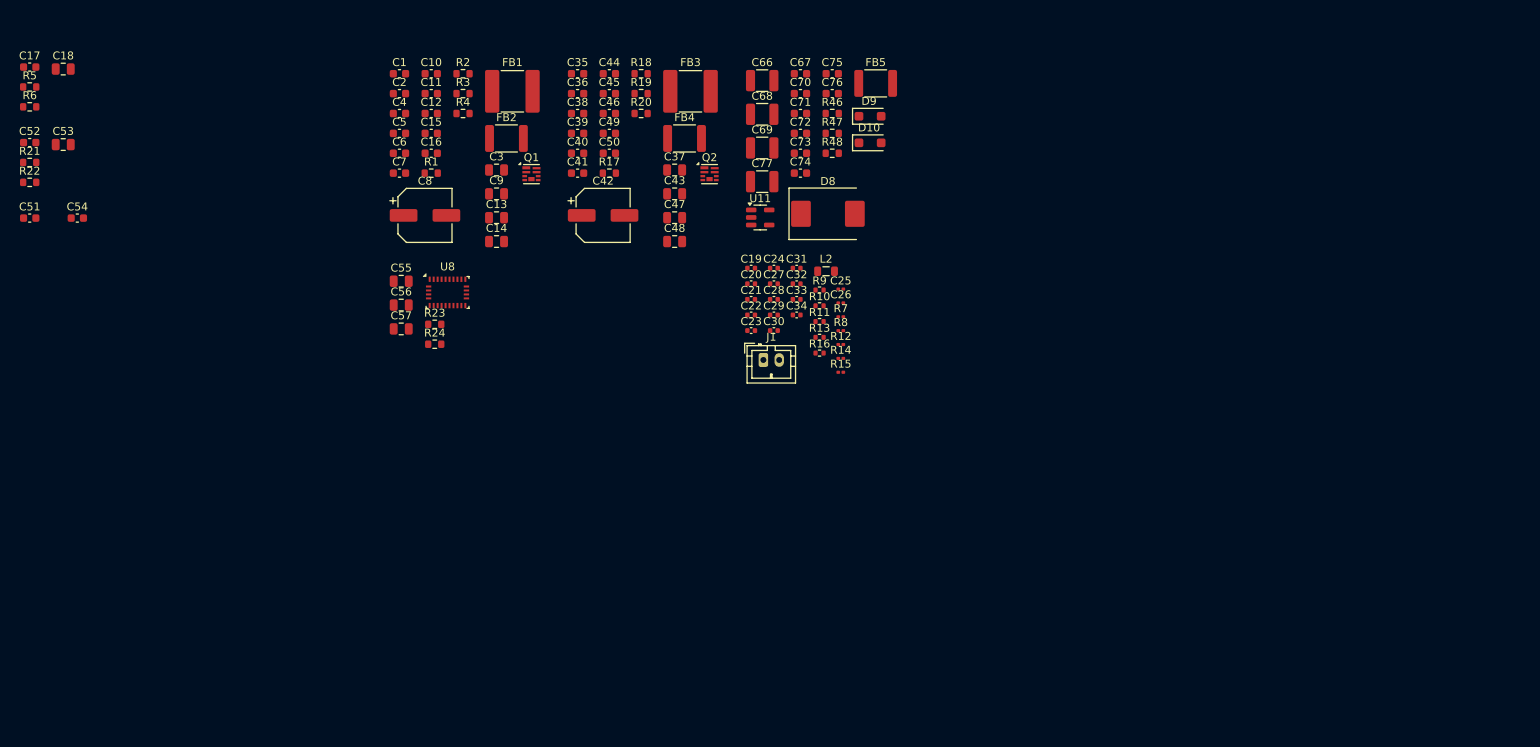
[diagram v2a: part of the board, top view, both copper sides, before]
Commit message: Doing placement for 5V 3V3 IMU
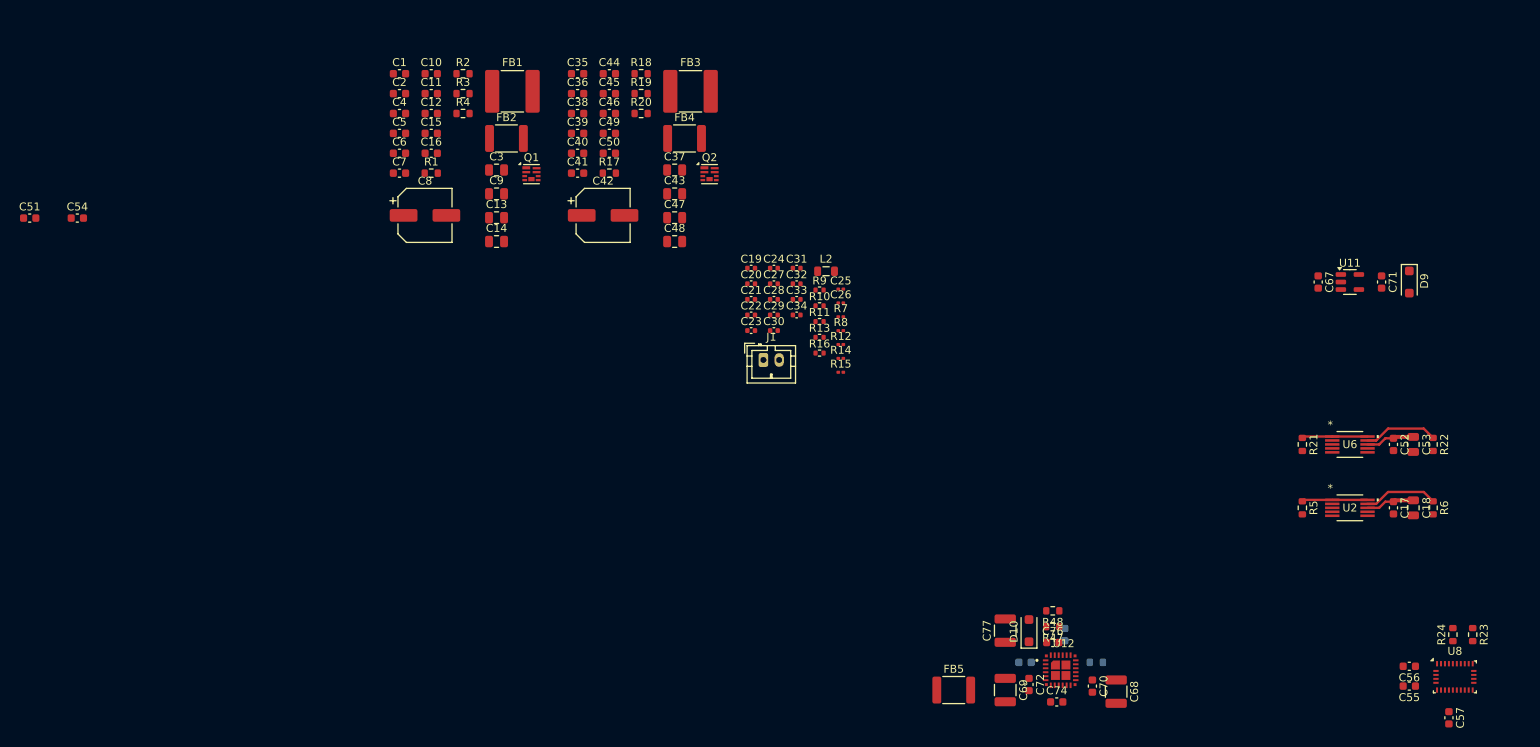
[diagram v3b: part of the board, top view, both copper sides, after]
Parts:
- removed C66: 10uf, Capacitor_SMD:C_1210_3225Metric
- removed D8: SMCJ26A, Diode_SMD:D_SMC
- added U12: LT8640SEV_PBF, _PowerBoard:CONV_LT8640SEV_PBF, F.Cu at (104.5, 126.5)
- added U2: AD5259BRMZ100, _PowerBoard:RM_10_ADI-M, F.Cu at (141.0, 106.0)
- added U6: AD5259BRMZ100, _PowerBoard:RM_10_ADI-M, F.Cu at (141.0, 98.0)
- C55, C56, C57: footprint Capacitor_SMD:C_0805_2012Metric -> Capacitor_SMD:C_0603_1608Metric
- C73, C75, R46: moved to B.Cu
- moved R6 184.2 mm to (151.5, 106.0), turned to -90 degrees
- moved C17 180.9 mm to (146.5, 106.0), turned to -90 degrees
- moved R22 180.2 mm to (151.5, 98.0), turned to -90 degrees
- moved C18 179.2 mm to (149.0, 106.0), turned to -90 degrees
- moved C52 176.3 mm to (146.5, 98.0), turned to -90 degrees
- moved C53 174.5 mm to (149.0, 98.0), turned to -90 degrees
- moved R5 169.2 mm to (135.0, 106.0), turned to -90 degrees
- moved R21 164.5 mm to (135.0, 98.0), turned to -90 degrees
- moved C57 141.0 mm to (153.5, 132.5), turned to -90 degrees
- moved C55 137.1 mm to (148.5, 128.5), turned to 180 degrees
- moved R23 136.7 mm to (156.5, 122.0), turned to -90 degrees
- moved U8 136.1 mm to (154.2, 127.3)
- moved C56 135.2 mm to (148.5, 126.0), turned to 180 degrees
- moved R24 133.6 mm to (154.0, 122.0), turned to 90 degrees
- moved C68 85.5 mm to (111.5, 129.2), turned to -90 degrees
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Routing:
- net +5V: track 0.00 -> 12.3 mm
- net Net-(U6-B): track 0.00 -> 9.38 mm
- net Net-(U2-B): track 0.00 -> 9.38 mm
- net Net-(U6-A): track 0.00 -> 8.30 mm
- net Net-(U2-A): track 0.00 -> 8.30 mm
